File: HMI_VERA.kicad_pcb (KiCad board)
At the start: 2 copper layers, 106 x 74 mm, 32 parts, among them J1 Conn_01x03, J2 Conn_01x03, J3 Conn_01x03, J4 Conn_01x03, J5 Conn_01x03, J6 Conn_01x03, J7 Conn_01x03, J8 Conn_01x03, J9 DB9_Female, U1 THD10-1211N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

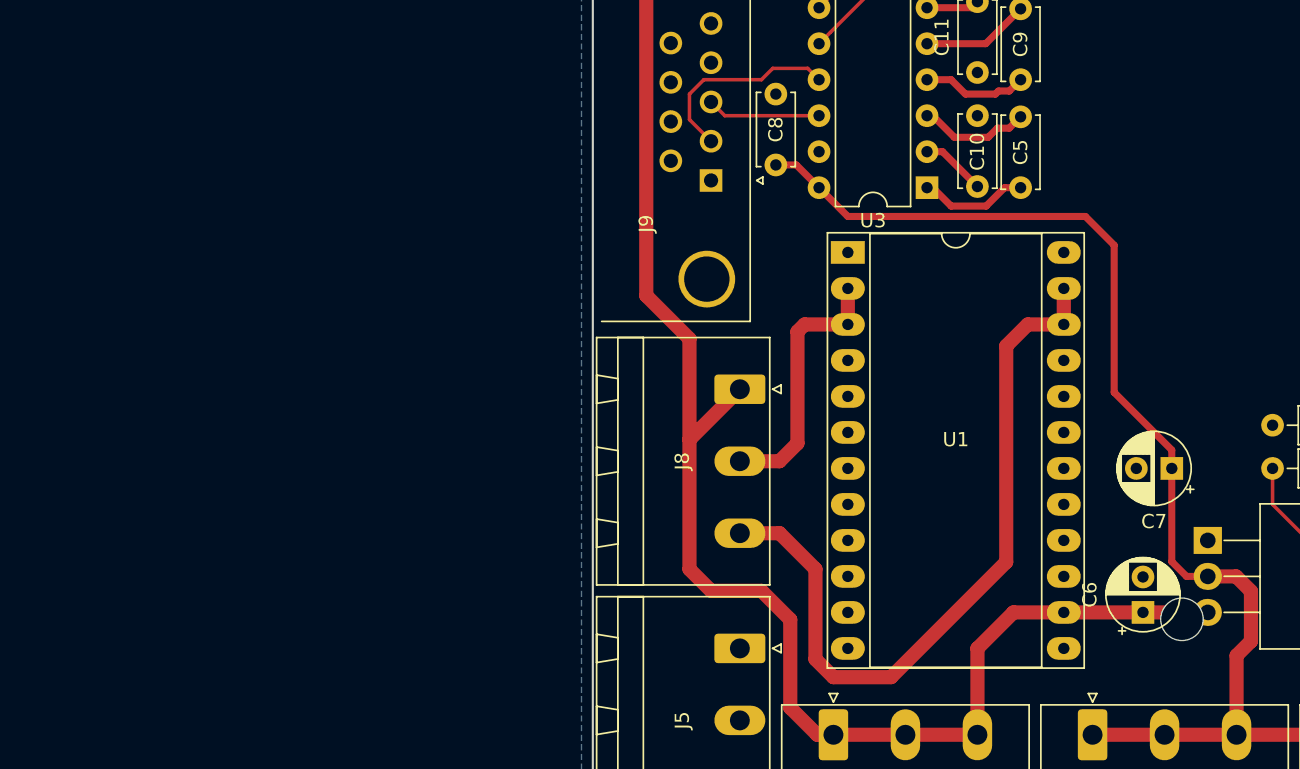
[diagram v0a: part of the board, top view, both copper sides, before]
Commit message: Remove unused connectors.
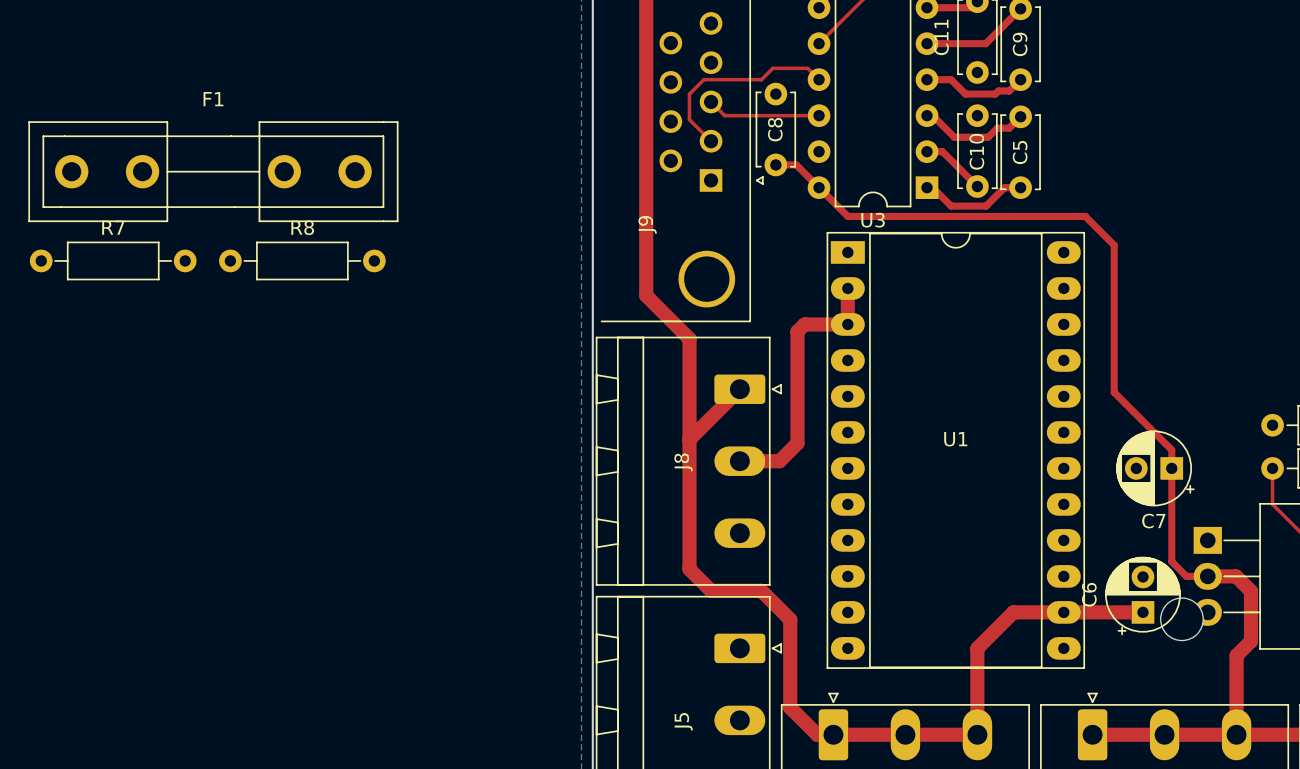
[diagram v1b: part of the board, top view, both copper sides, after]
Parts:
- added F1: 2A, Fuse_Holders_and_Fuses:Fuseholder5x20_horiz_open_inline_Type-I, F.Cu at (40.2, 81.7)
- added R7: 300k, Resistors_THT:R_Axial_DIN0207_L6.3mm_D2.5mm_P10.16mm_Horizontal, F.Cu at (38.1, 88.0)
- added R8: 100k, Resistors_THT:R_Axial_DIN0207_L6.3mm_D2.5mm_P10.16mm_Horizontal, F.Cu at (51.4, 88.0)
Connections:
- J8 pad 3: Net-(J8-Pad3) -> Net-(F1-Pad2)
- U1 pad 22: Net-(J8-Pad3) -> +BATT
- U1 pad 23: Net-(J8-Pad3) -> +BATT
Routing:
- net Net-(J8-Pad3): track 52.6 -> 0.00 mm
- net +5V: track 153.0 -> 148.4 mm

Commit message: Rev 2 completed
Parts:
- removed J5, J6, J7: Conn_01x03, Connector_Phoenix_MSTB:PhoenixContact_MSTBA_2,5_3-G-5,08_1x03_P5.08mm_Horizontal
- F1: footprint Fuse_Holders_and_Fuses:Fuseholder5x20_horiz_open_inline_Type-I -> Fuse_Holders_and_Fuses:BladeFuse-Mini
- J1, J2, J3, J4, J8: footprint Connector_Phoenix_MSTB:PhoenixContact_MSTBA_2,5_3-G-5,08_1x03_P5.08mm_Horizontal -> VeraHMI-PCB:205-15EDGRC-2.5-03P
- moved R7 82.4 mm to (120.4, 83.8), turned to 90 degrees
- moved R8 73.8 mm to (123.9, 73.8), turned to 270 degrees
- moved F1 53.2 mm to (88.5, 104.0), turned to 270 degrees
- moved U2 31.9 mm to (135.9, 79.8)
- moved C6 30.4 mm to (130.2, 86.0), turned to 270 degrees
- moved C7 24.9 mm to (130.2, 81.0), turned to 90 degrees
- moved R6 24.1 mm to (149.0, 104.2), turned to 90 degrees
- moved J3 21.2 mm to (150.0, 109.0)
- moved J8 18.1 mm to (101.0, 109.0), turned to 0 degrees
- moved R5 17.8 mm to (152.1, 94.1), turned to 270 degrees
- moved C1 17.0 mm to (129.1, 104.3)
- moved C2 17.0 mm to (135.7, 104.3)
- moved C3 17.0 mm to (142.3, 104.3)
- moved R1 17.0 mm to (132.1, 94.1)
- moved R3 17.0 mm to (145.3, 94.1)
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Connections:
- J2 pad 1: Net-(C3-Pad1) -> Net-(C2-Pad1)
- J2 pad 3: Net-(C2-Pad1) -> Net-(C3-Pad1)
- J4 pad 1: RUN -> Net-(J4-Pad1)
- J4 pad 3: Net-(J4-Pad3) -> RUN
- U4 pad 12: Net-(R5-Pad1) -> Net-(U4-Pad12)
- U4 pad 27: Net-(U4-Pad27) -> Net-(R5-Pad1)
- U4 pad 31: Net-(J4-Pad3) -> Net-(J4-Pad1)
- U4 pad 36: Net-(R7-Pad2) -> Net-(U4-Pad36)
- U4 pad 5: Net-(U4-Pad5) -> Net-(R7-Pad2)
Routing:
- net SpeedOmeter: track 53.4 -> 5.37 mm
- net Net-(J4-Pad1): track 0.00 -> 44.6 mm
- net +BATT: track 0.00 -> 44.2 mm
- net Net-(J4-Pad3): track 41.8 -> 0.00 mm
- net +5V: track 148.4 -> 176.6 mm
- net Net-(F1-Pad2): track 0.00 -> 17.2 mm
- net Net-(R3-Pad1): track 46.4 -> 31.0 mm
- net +3V3: track 142.3 -> 127.5 mm
- net RX: track 46.0 -> 59.9 mm
- net Net-(R4-Pad1): track 41.7 -> 29.2 mm
- net Net-(R7-Pad2): track 0.00 -> 12.2 mm
- net TX: track 46.4 -> 58.4 mm
- net Net-(C2-Pad1): track 20.0 -> 8.73 mm
- net Net-(J8-Pad2): track 18.8 -> 7.57 mm
- net Net-(R2-Pad1): track 44.7 -> 34.1 mm
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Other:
- board size 106 x 74 mm -> 100 x 60 mm
- net class Power added: clearance 0.2, trace_width 1, via_dia 0.8, via_drill 0.4

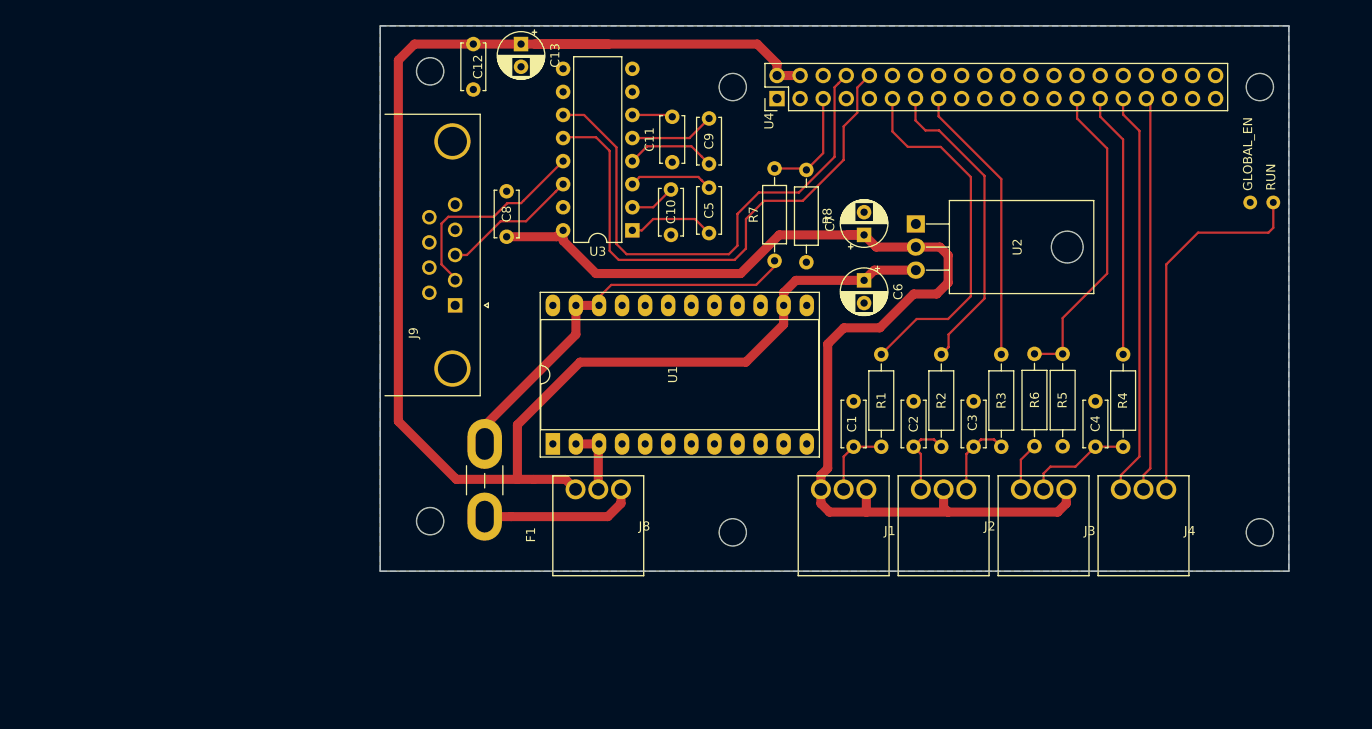
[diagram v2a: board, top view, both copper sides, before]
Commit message: Change voltage dividier input from BATT+ to 12V+.
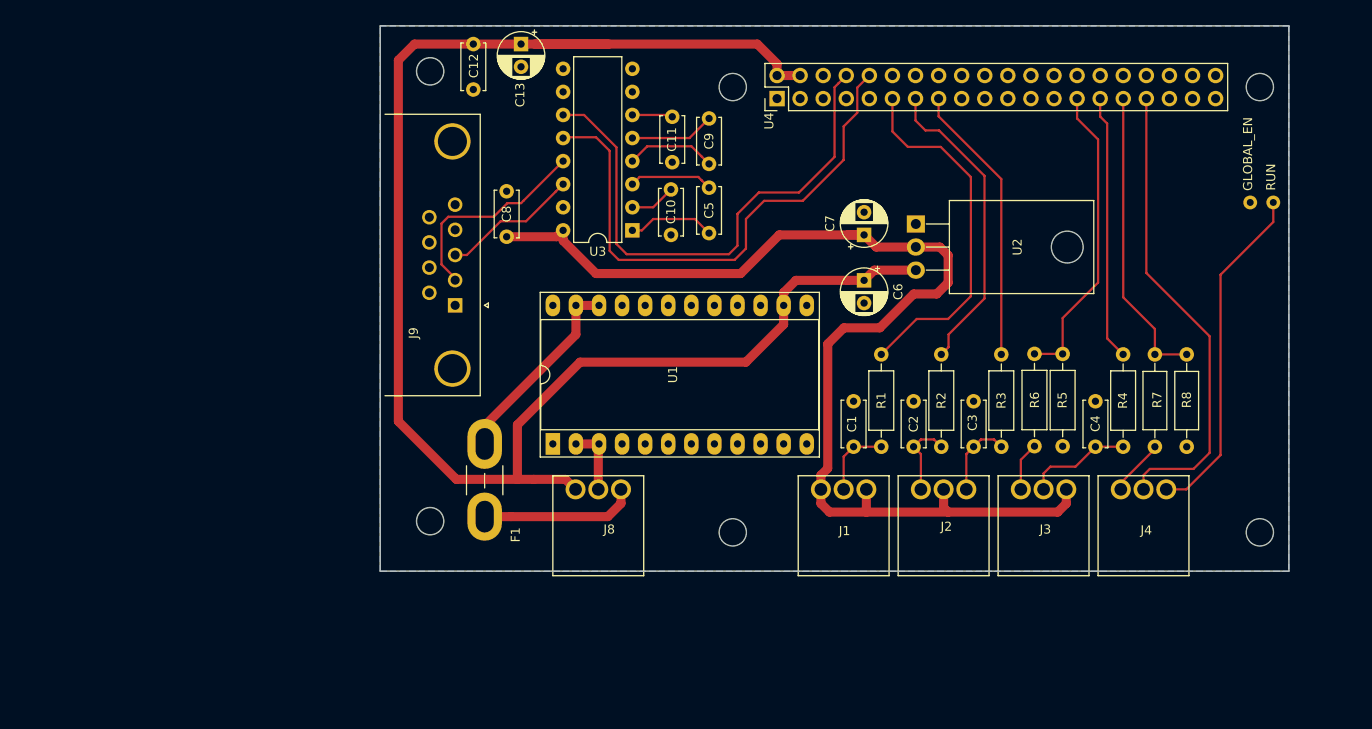
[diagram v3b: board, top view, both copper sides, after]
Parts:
- moved R8 46.5 mm to (165.8, 94.2)
- moved R7 43.1 mm to (162.2, 94.2), turned to 270 degrees
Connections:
- J4 pad 1: Net-(J4-Pad1) -> +12V
- R7 pad 1: +BATT -> Net-(R7-Pad1)
- R7 pad 2: Net-(R7-Pad2) -> +12V
- R8 pad 1: Net-(R7-Pad2) -> Net-(R7-Pad1)
- U4 pad 31: Net-(J4-Pad1) -> Net-(R7-Pad1)
- U4 pad 5: Net-(R7-Pad2) -> Net-(U4-Pad5)
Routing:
- net Net-(J4-Pad1): track 44.6 -> 0.00 mm
- net Net-(R7-Pad1): track 0.00 -> 33.1 mm
- net +BATT: track 44.2 -> 22.0 mm
- net Net-(R7-Pad2): track 12.2 -> 0.00 mm
- net Net-(J4-Pad2): track 43.5 -> 51.7 mm
- net +12V: track 0.00 -> 6.24 mm
- net RUN: track 41.0 -> 37.7 mm
- net Net-(R5-Pad1): track 34.6 -> 33.8 mm

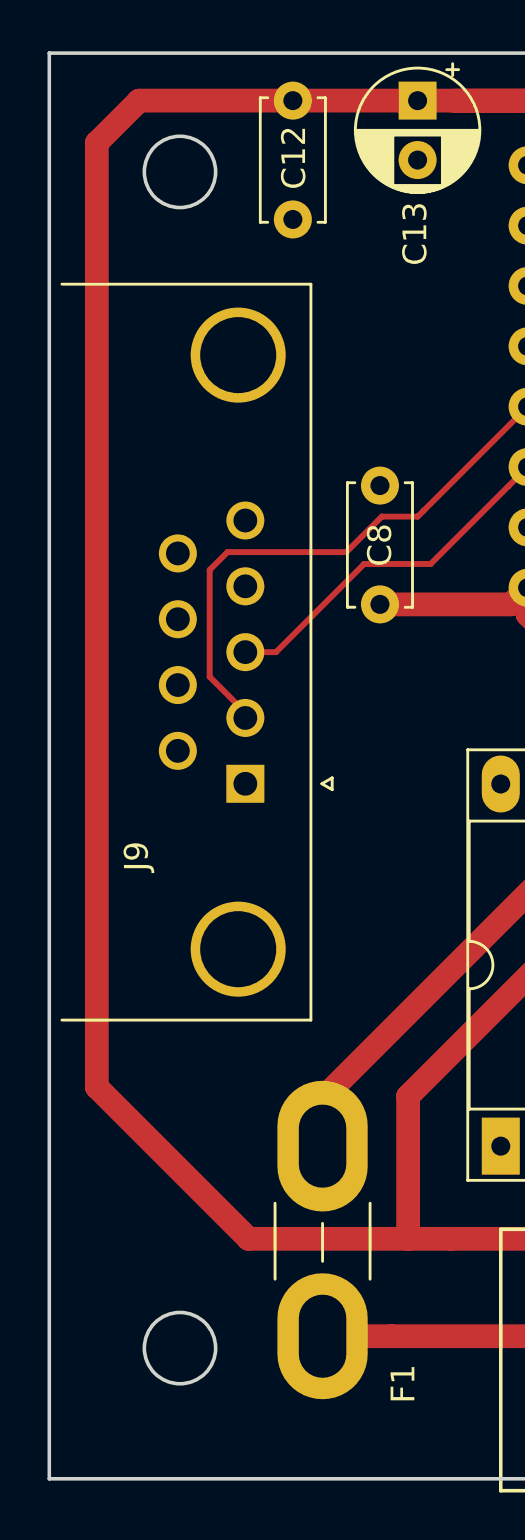
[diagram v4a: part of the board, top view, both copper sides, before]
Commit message: Change mouting holes from Edge cuts to footprint.
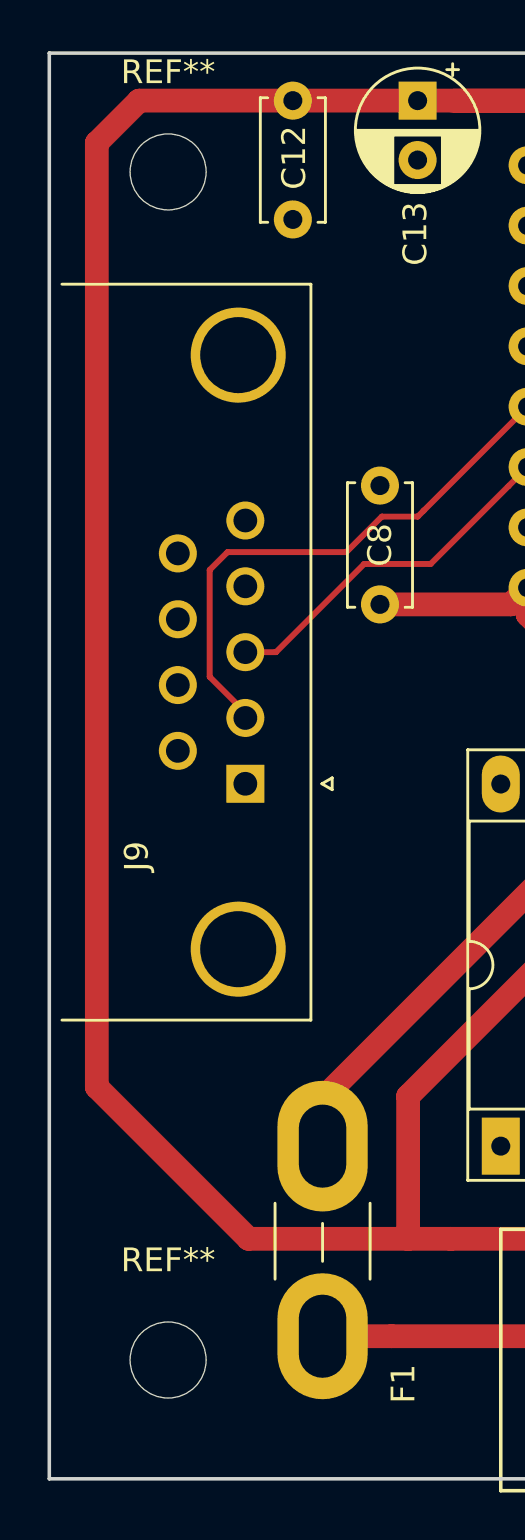
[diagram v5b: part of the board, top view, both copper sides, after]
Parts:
- added REF**: MountingHole_3.2mm_M3, Mounting_Holes:MountingHole_3.2mm_M3, F.Cu at (82.0, 113.0)
- added REF**: MountingHole_3.2mm_M3, Mounting_Holes:MountingHole_3.2mm_M3, F.Cu at (82.0, 63.0)
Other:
- outline, holes or cut-outs redrawn
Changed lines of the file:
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@@
   (general
     (thickness 1.6)
-    (drawings 8)
+    (drawings 6)
     (tracks 195)
     (zones 0)
-    (modules 32)
+    (modules 34)
     (nets 65)
   )
@@
     (add_net "Net-(J8-Pad2)")
   )
+  (module Mounting_Holes:MountingHole_3.2mm_M3 (layer F.Cu)
+    (at 82 113)
+    (descr "Mounting Hole 3.2mm, no annular, M3")
+    (tags "mounting hole 3.2mm no annular m3")
+    (attr virtual)
+    (fp_text reference REF** (at 0 -4.2) (layer F.SilkS)
+      (effects (font (size 1 1) (thickness 0.15)))
+    )
+    (fp_text value MountingHole_3.2mm_M3 (at 0 4.2) (layer F.Fab)
+      (effects (font (size 1 1) (thickness 0.15)))
+    )
+    (fp_text user %R (at 0.3 0) (layer F.Fab)
+      (effects (font (size 1 1) (thickness 0.15)))
+    )
+    (fp_circle (center 0 0) (end 3.2 0) (layer Cmts.User) (width 0.15))
+    (fp_circle (center 0 0) (end 3.45 0) (layer F.CrtYd) (width 0.05))
+    (pad 1 np_thru_hole circle (at 0 0) (size 3.2 3.2) (drill 3.2) (layers *.Cu *.Mask))
+  )
+  (module Mounting_Holes:MountingHole_3.2mm_M3 (layer F.Cu)
+    (at 82 63)
+    (descr "Mounting Hole 3.2mm, no annular, M3")
+    (tags "mounting hole 3.2mm no annular m3")
+    (attr virtual)
+    (fp_text reference REF** (at 0 -4.2) (layer F.SilkS)
+      (effects (font (size 1 1) (thickness 0.15)))
+    )
+    (fp_text value MountingHole_3.2mm_M3 (at 0 4.2) (layer F.Fab)
+      (effects (font (size 1 1) (thickness 0.15)))
+    )
+    (fp_text user %R (at 0.3 0) (layer F.Fab)
+      (effects (font (size 1 1) (thickness 0.15)))
+    )
+    (fp_circle (center 0 0) (end 3.2 0) (layer Cmts.User) (width 0.15))
+    (fp_circle (center 0 0) (end 3.45 0) (layer F.CrtYd) (width 0.05))
+    (pad 1 np_thru_hole circle (at 0 0) (size 3.2 3.2) (drill 3.2) (layers *.Cu *.Mask))
+  )
   (module Resistors_THT:R_Axial_DIN0207_L6.3mm_D2.5mm_P10.16mm_Horizontal (layer F.Cu)
     (at 165.75 94.15 270)
@@
     )
   )
-  (gr_circle (center 82.5 112.5) (end 82.5 114) (layer Edge.Cuts) (width 0.15))
-  (gr_circle (center 82.5 63) (end 82.5 61.5) (layer Edge.Cuts) (width 0.15))
   (gr_line (start 177 118) (end 177 58) (layer Edge.Cuts) (width 0.15))
   (gr_line (start 77 118) (end 177 118) (layer Edge.Cuts) (width 0.15))
